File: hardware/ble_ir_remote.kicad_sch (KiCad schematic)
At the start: 30 parts, among them Q1 MMBT3904, U1 ESP32-C3-MINI-1-N4

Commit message: sch progress
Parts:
- S1, S2, S3, S4, S5, S6, S7, S8: value TS-1187A-B -> (none)
- gave numbers to parts that had none: 1
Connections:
- net SW1 is gone; now on net SW_STANDBY: C1.1, R3.2
- net SW2 is gone; now on net SW_RESET: C2.1, R4.2
- net SW3 is gone; now on net SW_VOLP: C3.1, R5.2
- net SW4 is gone; now on net SW_VOLM: C4.1, R6.2
- net SW5 is gone; now on net SW_BASSP: C5.1, R7.2
- net SW6 is gone; now on net SW_BASSM: C6.1, R8.2
- net SW7 is gone; now on net SW_PROG1: C7.1, R9.2
- net SW8 is gone; now on net SW_PROG2: C8.1, R10.2
- net SW_STANDBY: now reaches U1.12 (IO0)
- net SW_RESET: now reaches U1.13 (IO1)
- net SW_PROG2: now reaches U1.16 (IO10)
- net SW_BASSP: now reaches U1.18 (IO4)
- net SW_BASSM: now reaches U1.19 (IO5)
- net SW_PROG1: now reaches U1.20 (IO6)
- net SW_VOLP: now reaches U1.5 (IO2)
- net SW_VOLM: now reaches U1.6 (IO3)
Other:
- note added: "Push buttons"
- moved on the sheet: C1, C2, C3, C4, C5, C6, C7, C8, R10, R3, R4, R5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

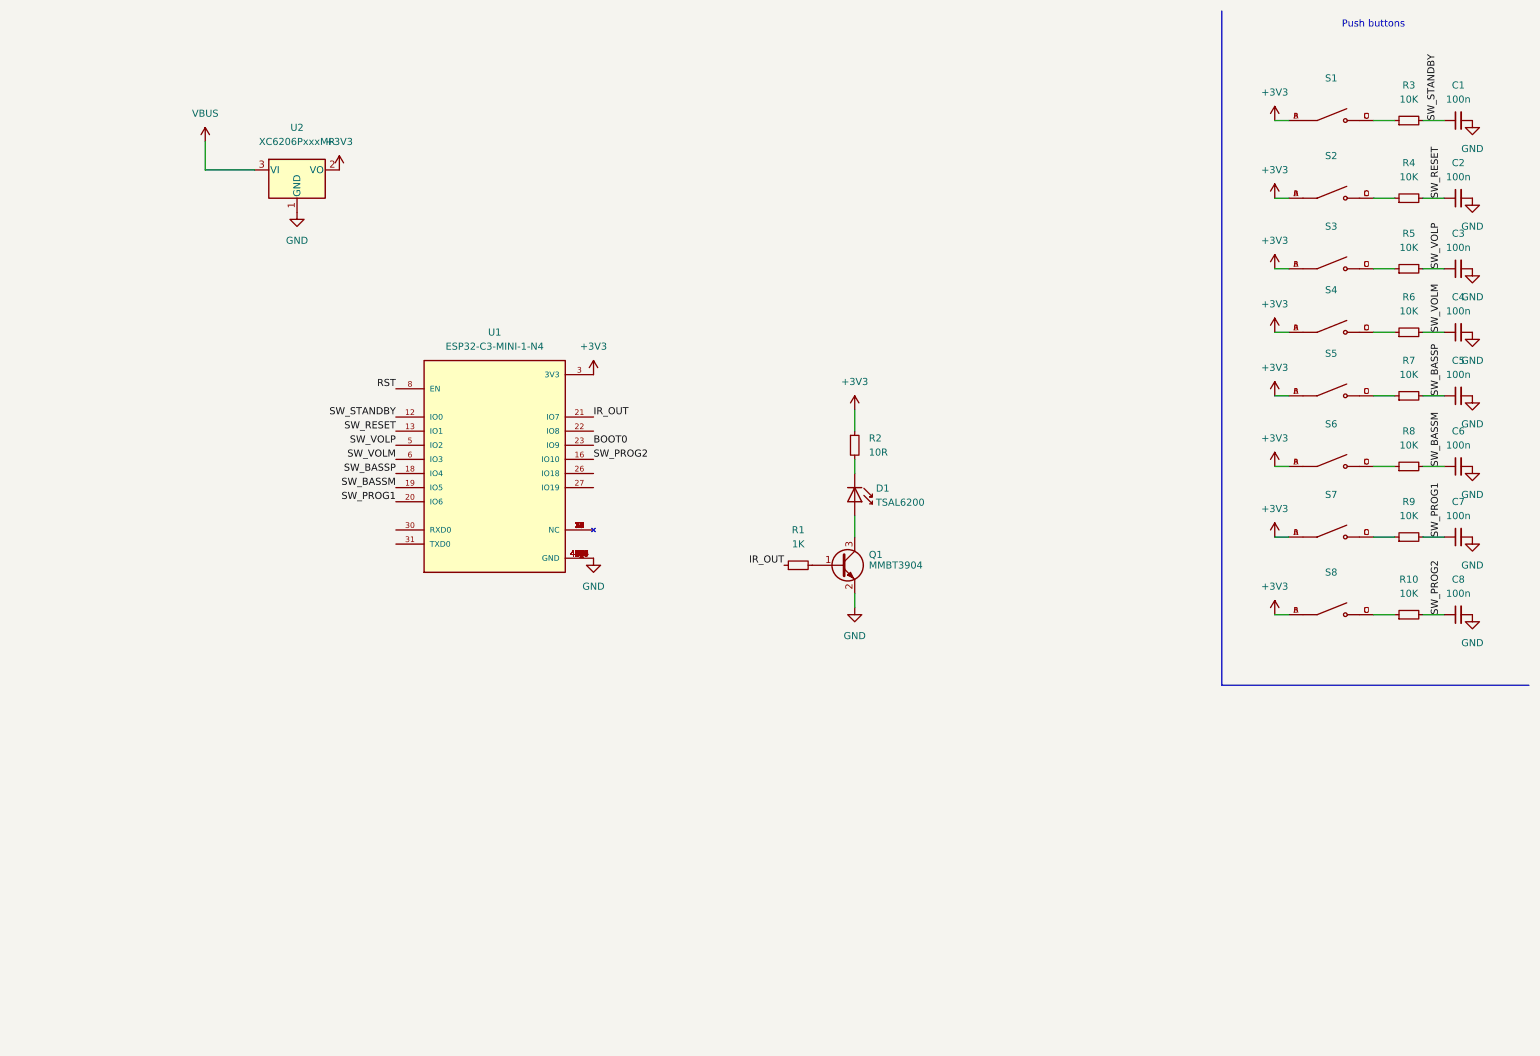
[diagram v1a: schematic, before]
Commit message: usb conn added
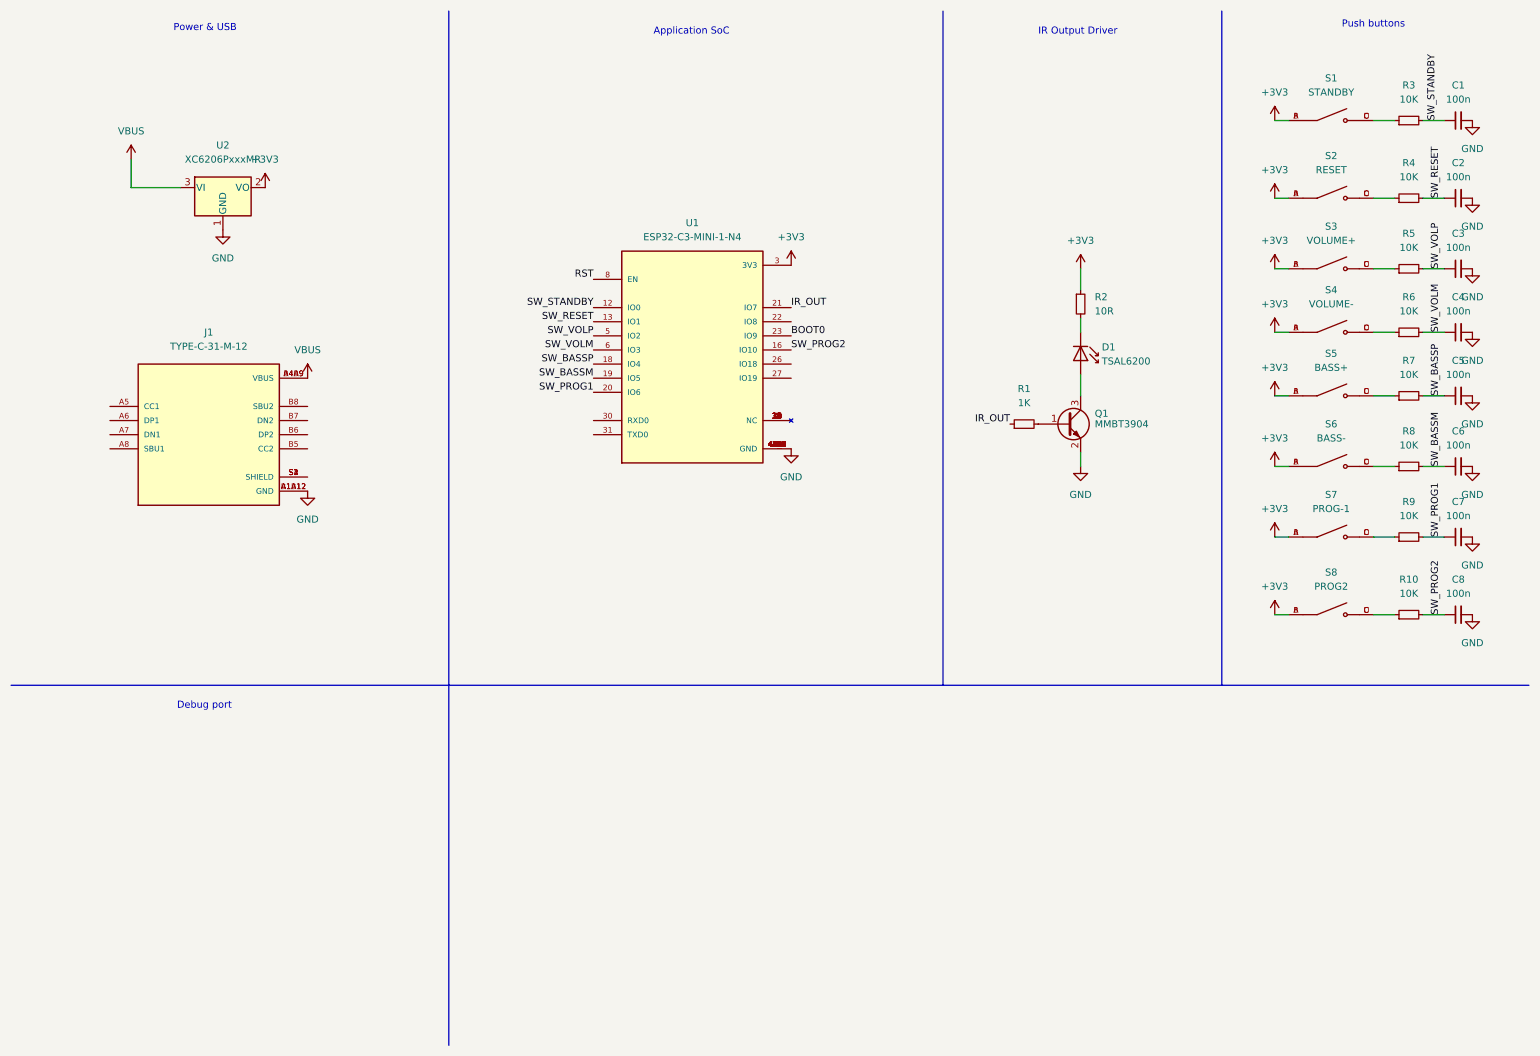
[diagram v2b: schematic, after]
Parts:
- added J1: TYPE-C-31-M-12, TYPE-C-31-M-12:HRO_TYPE-C-31-M-12, symbol TYPE-C-31-M-12:TYPE-C-31-M-12
- S1: value (none) -> STANDBY
- S2: value (none) -> RESET
- S3: value (none) -> VOLUME+
- S4: value (none) -> VOLUME-
- S5: value (none) -> BASS+
- S6: value (none) -> BASS-
- S7: value (none) -> PROG-1
- S8: value (none) -> PROG2
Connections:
- net GND: now also J1.A1B12 (GND), J1.B1A12 (GND)
- net VBUS: now also J1.A4B9 (VBUS), J1.B4A9 (VBUS)
- new net: J1.S1 (SHIELD), J1.S2 (SHIELD), J1.S3 (SHIELD), J1.S4 (SHIELD)
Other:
- note added: "Application SoC"
- note added: "Debug port"
- note added: "IR Output Driver"
- note added: "Power & USB"
- moved on the sheet: D1, Q1, R1, R2, U1, U2

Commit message: sch prgrs
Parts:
- added C10, C11, C12, C9: 100n, Capacitor_SMD:C_0603_1608Metric, symbol Device:C_Small
- added J2: Debug connector, symbol Connector:Conn_01x08_Male
- added R11, R12: 5.1K, Resistor_SMD:R_0603_1608Metric, symbol Device:R_Small
- J1: footprint TYPE-C-31-M-12:HRO_TYPE-C-31-M-12 -> HRO_TYPE-C-31-M-12
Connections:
- net +3V3: now also C10.2, C11.2, C12.2, J2.2 (Pin_2)
- net BOOT0: now also J2.6 (Pin_6)
- net GND: now also C10.1, C11.1, C12.1, C9.1, J2.8 (Pin_8), R11.1, R12.1
- net RST: now also J2.3 (Pin_3)
- net VBUS: now also C9.2, J2.1 (Pin_1)
- net at J1.A5 (CC1): now also R11.2
- net USB_D+: now reaches J1.A6 (DP1)
- net USB_D+: now also J1.B6 (DP2), U1.27 (IO19)
- net USB_D-: now reaches J1.A7 (DN1)
- net USB_D-: now also J1.B7 (DN2), U1.26 (IO18)
- net at J1.B5 (CC2): now also R12.2
- net BOOT1: now reaches U1.22 (IO8)
- net BOOT1: now also J2.7 (Pin_7)
- net RXD0: now reaches U1.30 (RXD0)
- net RXD0: now also J2.4 (Pin_4)
- net TXD0: now reaches U1.31 (TXD0)
- net TXD0: now also J2.5 (Pin_5)
- no-connect marks 0 -> 3

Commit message: sch prgs
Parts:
- added D2: (no value), symbol Device:LED_Small
- added R13: (no value), Resistor_SMD:R_0603_1608Metric, symbol Device:R_Small
- added R14: (no value), symbol Device:R_Small
- added U3: (no value), symbol Power_Protection:SRV05-4
- J2: value Debug connector -> (none)
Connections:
- net +3V3: now also R13.1, R14.1
- net BOOT1: now also D2.1 (K), R14.2
- net GND: now also U3.2 (VN)
- net USB_D+: now also U3.1 (IO1)
- net USB_D-: now also U3.3 (IO2)
- net VBUS: now also U3.5 (VP)
- new net: D2.2 (A), R13.2
- no-connect marks 3 -> 5
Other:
- moved on the sheet: C10, C9, J1, R11, R12, U2

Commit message: basic placement
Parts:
- C11, C9: value 100n -> (none)
- D2: value (none) -> Heartbeat; footprint (none) -> LED_SMD:LED_0603_1608Metric
- J2: value (none) -> Debug connector; footprint (none) -> Connector_PinHeader_2.54mm:PinHeader_1x08_P2.54mm_Vertical
- R13: value (none) -> 120R
- R14: value (none) -> 10K; footprint (none) -> Resistor_SMD:R_0603_1608Metric
- S1, S2, S3, S4, S5, S6, S7, S8: footprint TS-1187A-B-A-B:SW_TS-1187A-B-A-B -> SW_TS-1187A-B-A-B
- U1: value ESP32-C3-MINI-1-N4 -> (none); footprint ESP32-C3-MINI-1-N4:XCVR_ESP32-C3-MINI-1-N4 -> (none)
- U3: value (none) -> SRV05-4; footprint (none) -> Package_TO_SOT_SMD:SOT-23-6
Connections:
- no-connect marks 5 -> 4
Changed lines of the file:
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@@
   (no_connect (at 30.48 71.12))
   (no_connect (at 66.04 63.5))
-  (no_connect (at 152.4 85.725))
   (no_connect (at 61.595 109.855))
   (no_connect (at 61.595 104.775))
@@
       (effects (font (size 1.27 1.27)) (justify left))
     )
-    (property "Value" "" (id 1) (at 137.16 29.2099 0)
+    (property "Value" "120R" (id 1) (at 137.16 29.2099 0)
       (effects (font (size 1.27 1.27)) (justify left))
     )
@@
     (property "Reference" "S2" (id 0) (at 249.555 38.1 0))
     (property "Value" "RESET" (id 1) (at 249.555 40.64 0))
-    (property "Footprint" "TS-1187A-B-A-B:SW_TS-1187A-B-A-B" (id 2) (at 249.555 45.72 0)
+    (property "Footprint" "SW_TS-1187A-B-A-B" (id 2) (at 249.555 45.72 0)
       (effects (font (size 1.27 1.27)) (justify left bottom) hide)
     )
@@
   (symbol (lib_id "Device:C_Small") (at 128.27 108.585 180) (unit 1)
     (in_bom yes) (on_board yes) (fields_autoplaced)
-    (property "Reference" "C11" (id 0) (at 131.445 107.3085 0)
+    (property "Reference" "C11" (id 0) (at 130.81 107.3085 0)
       (effects (font (size 1.27 1.27)) (justify right))
     )
-    (property "Value" "100n" (id 1) (at 131.445 109.8485 0)
+    (property "Value" "" (id 1) (at 130.81 109.8485 0)
       (effects (font (size 1.27 1.27)) (justify right))
     )
@@
       (effects (font (size 1.27 1.27)) (justify left))
     )
-    (property "Value" "" (id 1) (at 147.955 37.465 90)
+    (property "Value" "Heartbeat" (id 1) (at 147.955 37.465 90)
       (effects (font (size 1.27 1.27)) (justify left))
     )
-    (property "Footprint" "" (id 2) (at 135.255 34.29 90)
-      (effects (font (size 1.27 1.27)) hide)
-    )
-    (property "Datasheet" "C2286" (id 3) (at 135.255 34.29 90)
+    (property "Footprint" "LED_SMD:LED_0603_1608Metric" (id 2) (at 135.255 34.29 90)
+      (effects (font (size 1.27 1.27)) hide)
+    )
+    (property "Datasheet" "~" (id 3) (at 135.255 34.29 90)
       (effects (font (size 1.27 1.27)) hide)
     )
@@
     (property "Reference" "S7" (id 0) (at 249.555 99.06 0))
     (property "Value" "PROG-1" (id 1) (at 249.555 101.6 0))
-    (property "Footprint" "TS-1187A-B-A-B:SW_TS-1187A-B-A-B" (id 2) (at 249.555 106.68 0)
+    (property "Footprint" "SW_TS-1187A-B-A-B" (id 2) (at 249.555 106.68 0)
       (effects (font (size 1.27 1.27)) (justify left bottom) hide)
     )
@@
       (effects (font (size 1.27 1.27)) (justify left))
     )
-    (property "Value" "" (id 1) (at 174.625 61.5949 0)
+    (property "Value" "10K" (id 1) (at 174.625 61.5949 0)
       (effects (font (size 1.27 1.27)) (justify left))
     )
-    (property "Footprint" "" (id 2) (at 172.085 60.325 0)
+    (property "Footprint" "Resistor_SMD:R_0603_1608Metric" (id 2) (at 172.085 60.325 0)
       (effects (font (size 1.27 1.27)) hide)
     )
@@
       (effects (font (size 1.27 1.27)) (justify left))
     )
-    (property "Value" "" (id 1) (at 51.6637 94.615 0)
+    (property "Value" "SRV05-4" (id 1) (at 51.6637 94.615 0)
       (effects (font (size 1.27 1.27)) (justify left))
     )
-    (property "Footprint" "" (id 2) (at 66.675 118.745 0)
+    (property "Footprint" "Package_TO_SOT_SMD:SOT-23-6" (id 2) (at 66.675 118.745 0)
       (effects (font (size 1.27 1.27)) hide)
     )
@@
     (property "Reference" "S6" (id 0) (at 249.555 86.36 0))
     (property "Value" "BASS-" (id 1) (at 249.555 88.9 0))
-    (property "Footprint" "TS-1187A-B-A-B:SW_TS-1187A-B-A-B" (id 2) (at 249.555 93.98 0)
+    (property "Footprint" "SW_TS-1187A-B-A-B" (id 2) (at 249.555 93.98 0)
       (effects (font (size 1.27 1.27)) (justify left bottom) hide)
     )
@@
     (property "Reference" "S1" (id 0) (at 249.555 24.13 0))
     (property "Value" "STANDBY" (id 1) (at 249.555 26.67 0))
-    (property "Footprint" "TS-1187A-B-A-B:SW_TS-1187A-B-A-B" (id 2) (at 249.555 31.75 0)
+    (property "Footprint" "SW_TS-1187A-B-A-B" (id 2) (at 249.555 31.75 0)
       (effects (font (size 1.27 1.27)) (justify left bottom) hide)
     )
@@
     (in_bom yes) (on_board yes) (fields_autoplaced)
     (property "Reference" "U1" (id 0) (at 134.62 50.165 0))
-    (property "Value" "ESP32-C3-MINI-1-N4" (id 1) (at 134.62 52.705 0))
-    (property "Footprint" "ESP32-C3-MINI-1-N4:XCVR_ESP32-C3-MINI-1-N4" (id 2) (at 134.62 73.025 0)
+    (property "Value" "" (id 1) (at 134.62 52.705 0))
+    (property "Footprint" "" (id 2) (at 134.62 73.025 0)
       (effects (font (size 1.27 1.27)) (justify left bottom) hide)
     )
@@
     (property "Reference" "S8" (id 0) (at 249.555 113.03 0))
     (property "Value" "PROG2" (id 1) (at 249.555 115.57 0))
-    (property "Footprint" "TS-1187A-B-A-B:SW_TS-1187A-B-A-B" (id 2) (at 249.555 120.65 0)
+    (property "Footprint" "SW_TS-1187A-B-A-B" (id 2) (at 249.555 120.65 0)
       (effects (font (size 1.27 1.27)) (justify left bottom) hide)
     )
@@
     (property "Reference" "S4" (id 0) (at 249.555 62.23 0))
     (property "Value" "VOLUME-" (id 1) (at 249.555 64.77 0))
-    (property "Footprint" "TS-1187A-B-A-B:SW_TS-1187A-B-A-B" (id 2) (at 249.555 69.85 0)
+    (property "Footprint" "SW_TS-1187A-B-A-B" (id 2) (at 249.555 69.85 0)
       (effects (font (size 1.27 1.27)) (justify left bottom) hide)
     )
@@
     (in_bom yes) (on_board yes) (fields_autoplaced)
     (property "Reference" "J2" (id 0) (at 46.355 149.86 0))
-    (property "Value" "" (id 1) (at 46.355 152.4 0))
-    (property "Footprint" "" (id 2) (at 45.72 163.195 0)
+    (property "Value" "Debug connector" (id 1) (at 46.355 152.4 0))
+    (property "Footprint" "Connector_PinHeader_2.54mm:PinHeader_1x08_P2.54mm_Vertical" (id 2) (at 45.72 163.195 0)
       (effects (font (size 1.27 1.27)) hide)
     )
@@
     (property "Reference" "S5" (id 0) (at 249.555 73.66 0))
     (property "Value" "BASS+" (id 1) (at 249.555 76.2 0))
-    (property "Footprint" "TS-1187A-B-A-B:SW_TS-1187A-B-A-B" (id 2) (at 249.555 81.28 0)
+    (property "Footprint" "SW_TS-1187A-B-A-B" (id 2) (at 249.555 81.28 0)
       (effects (font (size 1.27 1.27)) (justify left bottom) hide)
     )
@@
     (property "Reference" "S3" (id 0) (at 249.555 50.8 0))
     (property "Value" "VOLUME+" (id 1) (at 249.555 53.34 0))
-    (property "Footprint" "TS-1187A-B-A-B:SW_TS-1187A-B-A-B" (id 2) (at 249.555 58.42 0)
+    (property "Footprint" "SW_TS-1187A-B-A-B" (id 2) (at 249.555 58.42 0)
       (effects (font (size 1.27 1.27)) (justify left bottom) hide)
     )
@@
       (effects (font (size 1.27 1.27)) (justify right))
     )
-    (property "Value" "100n" (id 1) (at 34.29 33.0135 0)
+    (property "Value" "" (id 1) (at 34.29 33.0135 0)
       (effects (font (size 1.27 1.27)) (justify right))
     )
@@
     )
     (path "/fe42542b-46cc-4cf1-9215-2fddb7367389"
-      (reference "C9") (unit 1) (value "100n") (footprint "Capacitor_SMD:C_0603_1608Metric")
+      (reference "C9") (unit 1) (value "10u") (footprint "Capacitor_SMD:C_0603_1608Metric")
     )
     (path "/92978188-b801-41cd-b115-956dfb18afa1"
@@
     )
     (path "/1d2a07d1-a218-4de7-9cbf-1037a85d4f19"
-      (reference "C11") (unit 1) (value "100n") (footprint "Capacitor_SMD:C_0603_1608Metric")
+      (reference "C11") (unit 1) (value "10u") (footprint "Capacitor_SMD:C_0603_1608Metric")
     )
     (path "/0646904f-1c11-48e7-962b-72b8caf13ff9"
@@
     )
     (path "/8d4a48db-0e21-4b08-acf5-7ea1b1998675"
-      (reference "S1") (unit 1) (value "STANDBY") (footprint "TS-1187A-B-A-B:SW_TS-1187A-B-A-B")
+      (reference "S1") (unit 1) (value "STANDBY") (footprint "SW_TS-1187A-B-A-B")
     )
     (path "/070c67c3-5f08-4d00-882d-fd6b5081f42c"
-      (reference "S2") (unit 1) (value "RESET") (footprint "TS-1187A-B-A-B:SW_TS-1187A-B-A-B")
+      (reference "S2") (unit 1) (value "RESET") (footprint "SW_TS-1187A-B-A-B")
     )
     (path "/fdcb820d-b9bc-4b60-b223-6ddc09c6929d"
-      (reference "S3") (unit 1) (value "VOLUME+") (footprint "TS-1187A-B-A-B:SW_TS-1187A-B-A-B")
+      (reference "S3") (unit 1) (value "VOLUME+") (footprint "SW_TS-1187A-B-A-B")
     )
     (path "/c67ac3e4-b92d-4731-a29c-3aa570731610"
-      (reference "S4") (unit 1) (value "VOLUME-") (footprint "TS-1187A-B-A-B:SW_TS-1187A-B-A-B")
+      (reference "S4") (unit 1) (value "VOLUME-") (footprint "SW_TS-1187A-B-A-B")
     )
     (path "/f95a5364-1b21-4dfa-a4b5-d841e1a4f69a"
-      (reference "S5") (unit 1) (value "BASS+") (footprint "TS-1187A-B-A-B:SW_TS-1187A-B-A-B")
+      (reference "S5") (unit 1) (value "BASS+") (footprint "SW_TS-1187A-B-A-B")
     )
     (path "/8b219eba-2b62-4300-94e2-77b8510c1ff2"
-      (reference "S6") (unit 1) (value "BASS-") (footprint "TS-1187A-B-A-B:SW_TS-1187A-B-A-B")
+      (reference "S6") (unit 1) (value "BASS-") (footprint "SW_TS-1187A-B-A-B")
     )
     (path "/5c9b48ae-578a-48ac-8587-bbf011bcefac"
-      (reference "S7") (unit 1) (value "PROG-1") (footprint "TS-1187A-B-A-B:SW_TS-1187A-B-A-B")
+      (reference "S7") (unit 1) (value "PROG-1") (footprint "SW_TS-1187A-B-A-B")
     )
     (path "/c486cd04-ee3c-4ece-988c-6a297d5b401c"
-      (reference "S8") (unit 1) (value "PROG2") (footprint "TS-1187A-B-A-B:SW_TS-1187A-B-A-B")
+      (reference "S8") (unit 1) (value "PROG2") (footprint "SW_TS-1187A-B-A-B")
     )
     (path "/ab28c48c-701b-4892-a2b9-8b62bf64ab01"
-      (reference "U1") (unit 1) (value "ESP32-C3-MINI-1-N4") (footprint "ESP32-C3-MINI-1-N4:XCVR_ESP32-C3-MINI-1-N4")
+      (reference "U1") (unit 1) (value "ESP32-C3-MINI-1-N4") (footprint "XCVR_ESP32-C3-MINI-1-N4")
     )
     (path "/ed4e4948-02a0-455a-ad8c-7a6e3eaafe56"
